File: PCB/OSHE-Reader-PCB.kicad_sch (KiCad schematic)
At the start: 2 parts

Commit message: Update OSHE-Reader-PCB.kicad_sch
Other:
- sheet Display Connector ports: added GND; removed none
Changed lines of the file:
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@@
+	(symbol
+		(lib_id "power:GND")
+		(at 99.06 71.12 0)
+		(unit 1)
+		(exclude_from_sim no)
+		(in_bom yes)
+		(on_board yes)
+		(dnp no)
+		(fields_autoplaced yes)
+		(property "Reference" "#PWR011"
+			(at 99.06 77.47 0)
+			(effects
+				(font
+					(size 1.27 1.27)
+				)
+				(hide yes)
+			)
+		)
+		(property "Value" "GND"
+			(at 99.06 76.2 0)
+			(effects
+				(font
+					(size 1.27 1.27)
+				)
+			)
+		)
+		(property "Footprint" ""
+			(at 99.06 71.12 0)
+			(effects
+				(font
+					(size 1.27 1.27)
+				)
+				(hide yes)
+			)
+		)
+		(property "Datasheet" ""
+			(at 99.06 71.12 0)
+			(effects
+				(font
+					(size 1.27 1.27)
+				)
+				(hide yes)
+			)
+		)
+		(property "Description" "Power symbol creates a global label with name \"GND\" , ground"
+			(at 99.06 71.12 0)
+			(effects
+				(font
+					(size 1.27 1.27)
+				)
+				(hide yes)
+			)
+		)
+		(pin "1"
+		)
+		(instances
+			(project ""
+				(path "/3f072c92-e35a-4654-839b-728bd3dc3a46"
+					(reference "#PWR011")
+					(unit 1)
+				)
+			)
+		)
+	)
 	(symbol
 		(lib_id "power:GND")
@@
 			)
 		)
+		(pin "GND" input
+			(at 103.505 64.77 180)
+			(effects
+				(font
+					(size 1.27 1.27)
+				)
+				(justify left)
+			)
+		)

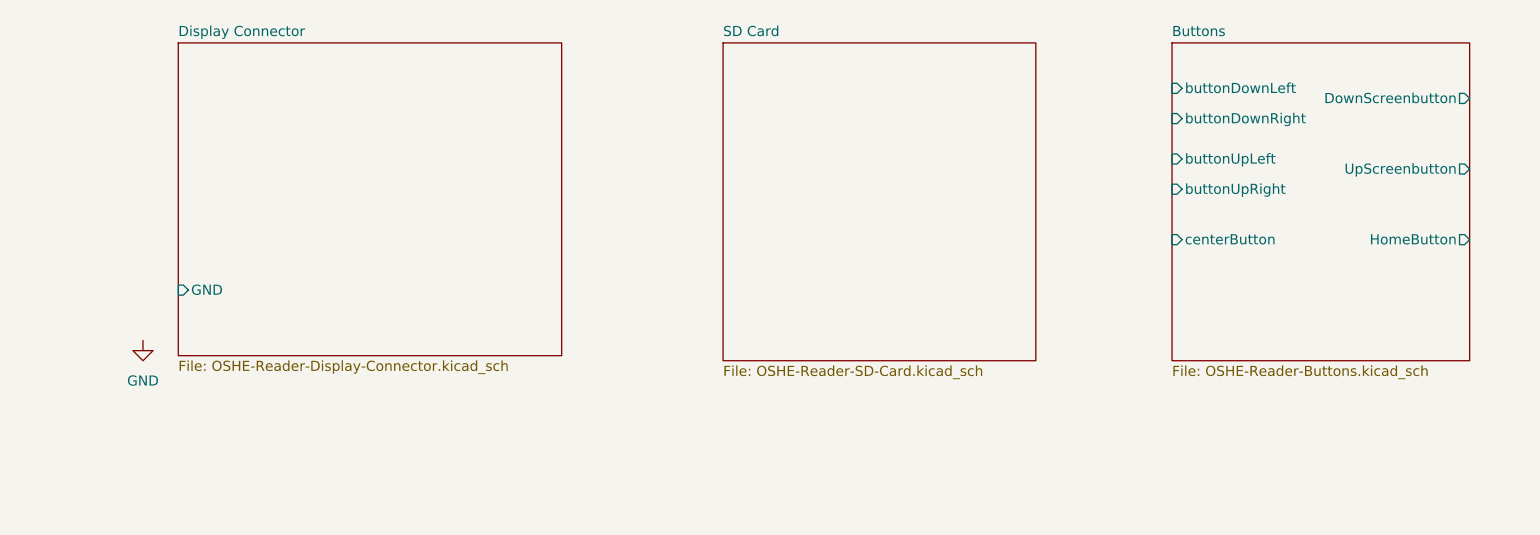
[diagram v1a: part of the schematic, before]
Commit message: Updating pins in roots file
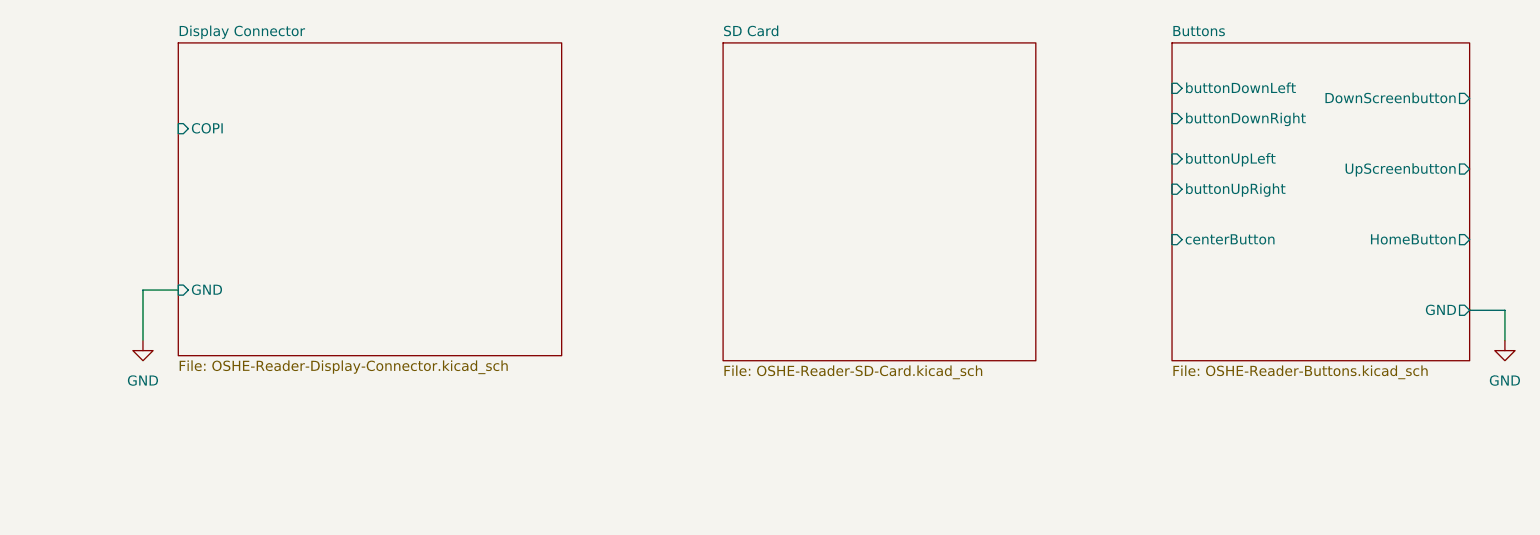
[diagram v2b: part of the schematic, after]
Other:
- sheet Buttons ports: added GND; removed none
- sheet Display Connector ports: added COPI; removed none
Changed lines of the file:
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@@
+	(wire
+		(pts
+			(xy 99.06 64.77) (xy 103.505 64.77)
+		)
+		(stroke
+			(width 0)
+			(type default)
+		)
+	)
 	(wire
 		(pts
@@
 	(wire
 		(pts
+			(xy 270.51 71.12) (xy 270.51 67.31)
+		)
+		(stroke
+			(width 0)
+			(type default)
+		)
+	)
+	(wire
+		(pts
 			(xy 90.17 166.37) (xy 92.71 166.37)
 		)
@@
 	(wire
 		(pts
+			(xy 99.06 64.77) (xy 99.06 71.12)
+		)
+		(stroke
+			(width 0)
+			(type default)
+		)
+	)
+	(wire
+		(pts
 			(xy 104.14 137.16) (xy 101.6 137.16)
 		)
@@
 		(pts
 			(xy 154.94 137.16) (xy 157.48 137.16)
+		)
+		(stroke
+			(width 0)
+			(type default)
+		)
+	)
+	(wire
+		(pts
+			(xy 270.51 67.31) (xy 266.065 67.31)
 		)
 		(stroke
@@
 	(symbol
 		(lib_id "power:GND")
+		(at 270.51 71.12 0)
+		(unit 1)
+		(exclude_from_sim no)
+		(in_bom yes)
+		(on_board yes)
+		(dnp no)
+		(fields_autoplaced yes)
+		(property "Reference" "#PWR06"
+			(at 270.51 77.47 0)
+			(effects
+				(font
+					(size 1.27 1.27)
+				)
+				(hide yes)
+			)
+		)
+		(property "Value" "GND"
+			(at 270.51 76.2 0)
+			(effects
+				(font
+					(size 1.27 1.27)
+				)
+			)
+		)
+		(property "Footprint" ""
+			(at 270.51 71.12 0)
+			(effects
+				(font
+					(size 1.27 1.27)
+				)
+				(hide yes)
+			)
+		)
+		(property "Datasheet" ""
+			(at 270.51 71.12 0)
+			(effects
+				(font
+					(size 1.27 1.27)
+				)
+				(hide yes)
+			)
+		)
+		(property "Description" "Power symbol creates a global label with name \"GND\" , ground"
+			(at 270.51 71.12 0)
+			(effects
+				(font
+					(size 1.27 1.27)
+				)
+				(hide yes)
+			)
+		)
+		(pin "1"
+		)
+		(instances
+			(project "OSHE-Reader-PCB"
+				(path "/3f072c92-e35a-4654-839b-728bd3dc3a46"
+					(reference "#PWR06")
+					(unit 1)
+				)
+			)
+		)
+	)
+	(symbol
+		(lib_id "power:GND")
 		(at 101.6 139.7 0)
 		(unit 1)
@@
 			)
 		)
+		(pin "GND" output
+			(at 266.065 67.31 0)
+			(effects
+				(font
+					(size 1.27 1.27)
+				)
+				(justify right)
+			)
+		)
 		(instances
 			(project "OSHE-Reader-PCB"
@@
 			(effects
 				(font
+					(size 1.27 1.27)
+				)
+				(justify left)
+			)
+		)
+		(pin "COPI" input
+			(at 103.505 44.45 180)
+			(effects
+				(font

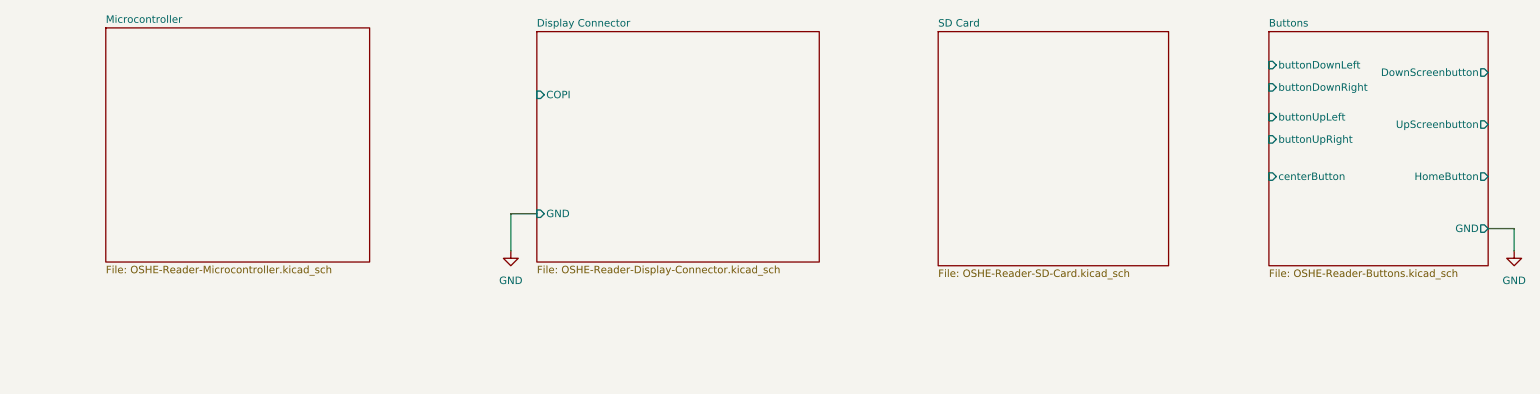
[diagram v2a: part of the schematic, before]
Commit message: updated sd card main sheet pins, swapped big caps for small ones on display connector for better readability
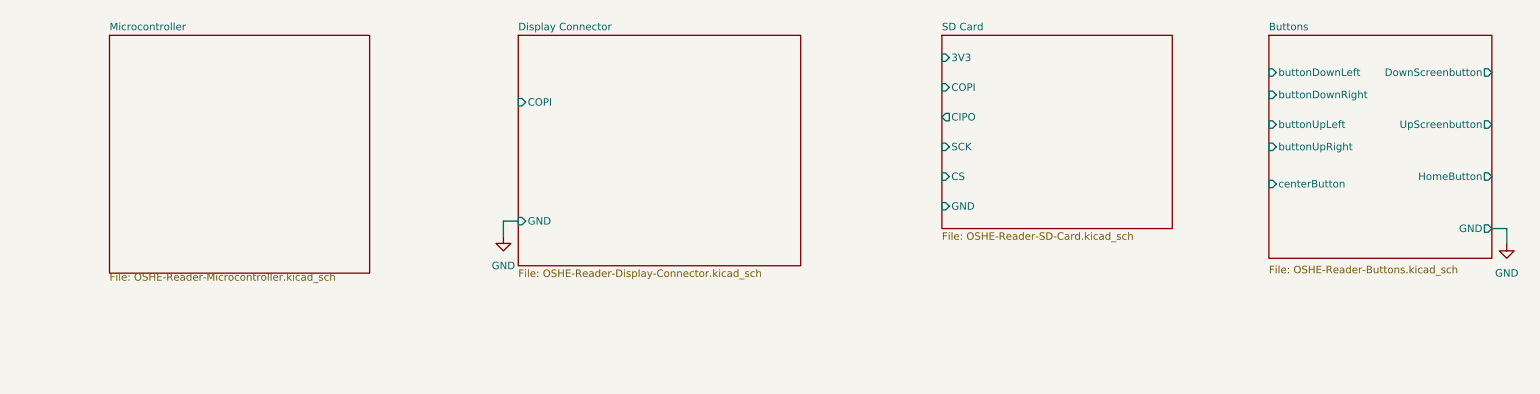
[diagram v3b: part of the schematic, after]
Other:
- sheet SD Card ports: added 3V3, CIPO, COPI, CS, GND, SCK; removed none
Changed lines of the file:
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@@
+	(wire
+		(pts
+			(xy 269.24 67.31) (xy 266.7 67.31)
+		)
+		(stroke
+			(width 0)
+			(type default)
+		)
+	)
 	(wire
 		(pts
@@
 	(wire
 		(pts
-			(xy 99.06 64.77) (xy 103.505 64.77)
-		)
-		(stroke
-			(width 0)
-			(type default)
-		)
-	)
-	(wire
-		(pts
 			(xy 87.63 166.37) (xy 87.63 162.56)
 		)
@@
 	(wire
 		(pts
+			(xy 100.33 66.04) (xy 97.79 66.04)
+		)
+		(stroke
+			(width 0)
+			(type default)
+		)
+	)
+	(wire
+		(pts
 			(xy 87.63 154.94) (xy 87.63 129.54)
 		)
@@
 	(wire
 		(pts
+			(xy 269.24 69.85) (xy 269.24 67.31)
+		)
+		(stroke
+			(width 0)
+			(type default)
+		)
+	)
+	(wire
+		(pts
 			(xy 30.48 137.16) (xy 33.02 137.16)
 		)
@@
 	(wire
 		(pts
-			(xy 270.51 71.12) (xy 270.51 67.31)
-		)
-		(stroke
-			(width 0)
-			(type default)
-		)
-	)
-	(wire
-		(pts
 			(xy 90.17 166.37) (xy 92.71 166.37)
 		)
@@
 	(wire
 		(pts
-			(xy 99.06 64.77) (xy 99.06 71.12)
-		)
-		(stroke
-			(width 0)
-			(type default)
-		)
-	)
-	(wire
-		(pts
 			(xy 104.14 137.16) (xy 101.6 137.16)
 		)
@@
 	(wire
 		(pts
-			(xy 270.51 67.31) (xy 266.065 67.31)
+			(xy 97.79 66.04) (xy 97.79 68.58)
 		)
 		(stroke
@@
 	(symbol
 		(lib_id "power:GND")
-		(at 99.06 71.12 0)
+		(at 97.79 68.58 0)
 		(unit 1)
 		(exclude_from_sim no)
@@
 		(fields_autoplaced yes)
 		(property "Reference" "#PWR011"
-			(at 99.06 77.47 0)
+			(at 97.79 74.93 0)
 			(effects
 				(font
@@
 		)
 		(property "Value" "GND"
-			(at 99.06 76.2 0)
+			(at 97.79 73.66 0)
 			(effects
 				(font
@@
 		)
 		(property "Footprint" ""
-			(at 99.06 71.12 0)
+			(at 97.79 68.58 0)
 			(effects
 				(font
@@
 		)
 		(property "Datasheet" ""
-			(at 99.06 71.12 0)
+			(at 97.79 68.58 0)
 			(effects
 				(font
@@
 		)
 		(property "Description" "Power symbol creates a global label with name \"GND\" , ground"
-			(at 99.06 71.12 0)
+			(at 97.79 68.58 0)
 			(effects
 				(font
@@
 	(symbol
 		(lib_id "power:GND")
-		(at 270.51 71.12 0)
+		(at 269.24 69.85 0)
 		(unit 1)
 		(exclude_from_sim no)
@@
 		(fields_autoplaced yes)
 		(property "Reference" "#PWR06"
-			(at 270.51 77.47 0)
+			(at 269.24 76.2 0)
 			(effects
 				(font
@@
 		)
 		(property "Value" "GND"
-			(at 270.51 76.2 0)
+			(at 269.24 74.93 0)
 			(effects
 				(font
@@
 		)
 		(property "Footprint" ""
-			(at 270.51 71.12 0)
+			(at 269.24 69.85 0)
 			(effects
 				(font
@@
 		)
 		(property "Datasheet" ""
-			(at 270.51 71.12 0)
+			(at 269.24 69.85 0)
 			(effects
 				(font
@@
 		)
 		(property "Description" "Power symbol creates a global label with name \"GND\" , ground"
-			(at 270.51 71.12 0)
+			(at 269.24 69.85 0)
 			(effects
 				(font
@@
 	)
 	(sheet
-		(at 29.845 33.02)
-		(size 45.085 40.005)
+		(at 30.48 34.29)
+		(size 44.45 40.64)
 		(exclude_from_sim no)
 		(in_bom yes)
@@
 		)
 		(property "Sheetname" "Microcontroller"
-			(at 29.845 32.3084 0)
+			(at 30.48 33.5784 0)
 			(effects
 				(font
@@
 		)
 		(property "Sheetfile" "OSHE-Reader-Microcontroller.kicad_sch"
-			(at 29.845 73.6096 0)
+			(at 30.48 74.8796 0)
 			(effects
 				(font
@@
 	)
 	(sheet
-		(at 228.6 33.655)
-		(size 37.465 40.005)
+		(at 228.6 34.29)
+		(size 38.1 38.1)
 		(exclude_from_sim no)
 		(in_bom yes)
@@
 		)
 		(property "Sheetname" "Buttons"
-			(at 228.6 32.9434 0)
+			(at 228.6 33.5784 0)
 			(effects
 				(font
@@
 		)
 		(property "Sheetfile" "OSHE-Reader-Buttons.kicad_sch"
-			(at 228.6 74.2446 0)
+			(at 228.6 73.6096 0)
 			(effects
 				(font
@@
 		)
 		(pin "buttonDownLeft" input
-			(at 228.6 39.37 180)
+			(at 228.6 40.64 180)
 			(effects
 				(font
@@
 		)
 		(pin "buttonUpLeft" input
-			(at 228.6 48.26 180)
+			(at 228.6 49.53 180)
 			(effects
 				(font
@@
 		)
 		(pin "centerButton" input
-			(at 228.6 58.42 180)
+			(at 228.6 59.69 180)
 			(effects
 				(font
@@
 		)
 		(pin "buttonDownRight" input
-			(at 228.6 43.18 180)
+			(at 228.6 44.45 180)
 			(effects
 				(font
@@
 		)
 		(pin "buttonUpRight" input
-			(at 228.6 52.07 180)
+			(at 228.6 53.34 180)
 			(effects
 				(font
@@
 		)
 		(pin "DownScreenbutton" output
-			(at 266.065 40.64 0)
+			(at 266.7 40.64 0)
 			(effects
 				(font
@@
 		)
 		(pin "HomeButton" output
-			(at 266.065 58.42 0)
+			(at 266.7 58.42 0)
 			(effects
 				(font
@@
 		)
 		(pin "UpScreenbutton" output
-			(at 266.065 49.53 0)
+			(at 266.7 49.53 0)
 			(effects
 				(font
@@
 		)
 		(pin "GND" output
-			(at 266.065 67.31 0)
+			(at 266.7 67.31 0)
 			(effects
 				(font
@@
 	)
 	(sheet
-		(at 103.505 33.655)
+		(at 100.33 34.29)
 		(size 48.26 39.37)
 		(exclude_from_sim no)
@@
 		)
 		(property "Sheetname" "Display Connector"
-			(at 103.505 32.9434 0)
+			(at 100.33 33.5784 0)
 			(effects
 				(font
@@
 		)
 		(property "Sheetfile" "OSHE-Reader-Display-Connector.kicad_sch"
-			(at 103.505 73.6096 0)
+			(at 100.33 74.2446 0)
 			(effects
 				(font
@@
 		)
 		(pin "GND" input
-			(at 103.505 64.77 180)
+			(at 100.33 66.04 180)
 			(effects
 				(font
@@
 		)
 		(pin "COPI" input
-			(at 103.505 44.45 180)
+			(at 100.33 45.72 180)
 			(effects
 				(font
@@
 	)
 	(sheet
-		(at 172.085 33.655)
-		(size 39.37 40.005)
+		(at 172.72 34.29)
+		(size 39.37 33.02)
 		(exclude_from_sim no)
 		(in_bom yes)
@@
 		)
 		(property "Sheetname" "SD Card"
-			(at 172.085 32.9434 0)
+			(at 172.72 33.5784 0)
 			(effects
 				(font
@@
 		)
 		(property "Sheetfile" "OSHE-Reader-SD-Card.kicad_sch"
-			(at 172.085 74.2446 0)
+			(at 172.72 67.8946 0)
 			(effects
 				(font
@@
 			)
 		)
+		(pin "CS" input
+			(at 172.72 58.42 180)
+			(effects
+				(font
+					(size 1.27 1.27)
+				)
+				(justify left)
+			)
+		)
+		(pin "SCK" input
+			(at 172.72 53.34 180)
+			(effects
+				(font
+					(size 1.27 1.27)
+				)
+				(justify left)
+			)
+		)
+		(pin "3V3" input
+			(at 172.72 38.1 180)
+			(effects
+				(font
+					(size 1.27 1.27)
+				)
+				(justify left)
+			)
+		)
+		(pin "CIPO" output
+			(at 172.72 48.26 180)
+			(effects
+				(font
+					(size 1.27 1.27)
+				)
+				(justify left)
+			)
+		)
+		(pin "COPI" input
+			(at 172.72 43.18 180)
+			(effects
+				(font
+					(size 1.27 1.27)
+				)
+				(justify left)
+			)
+		)
+		(pin "GND" input
+			(at 172.72 63.5 180)
+			(effects
+				(font
+					(size 1.27 1.27)
+				)
+				(justify left)
+			)
+		)

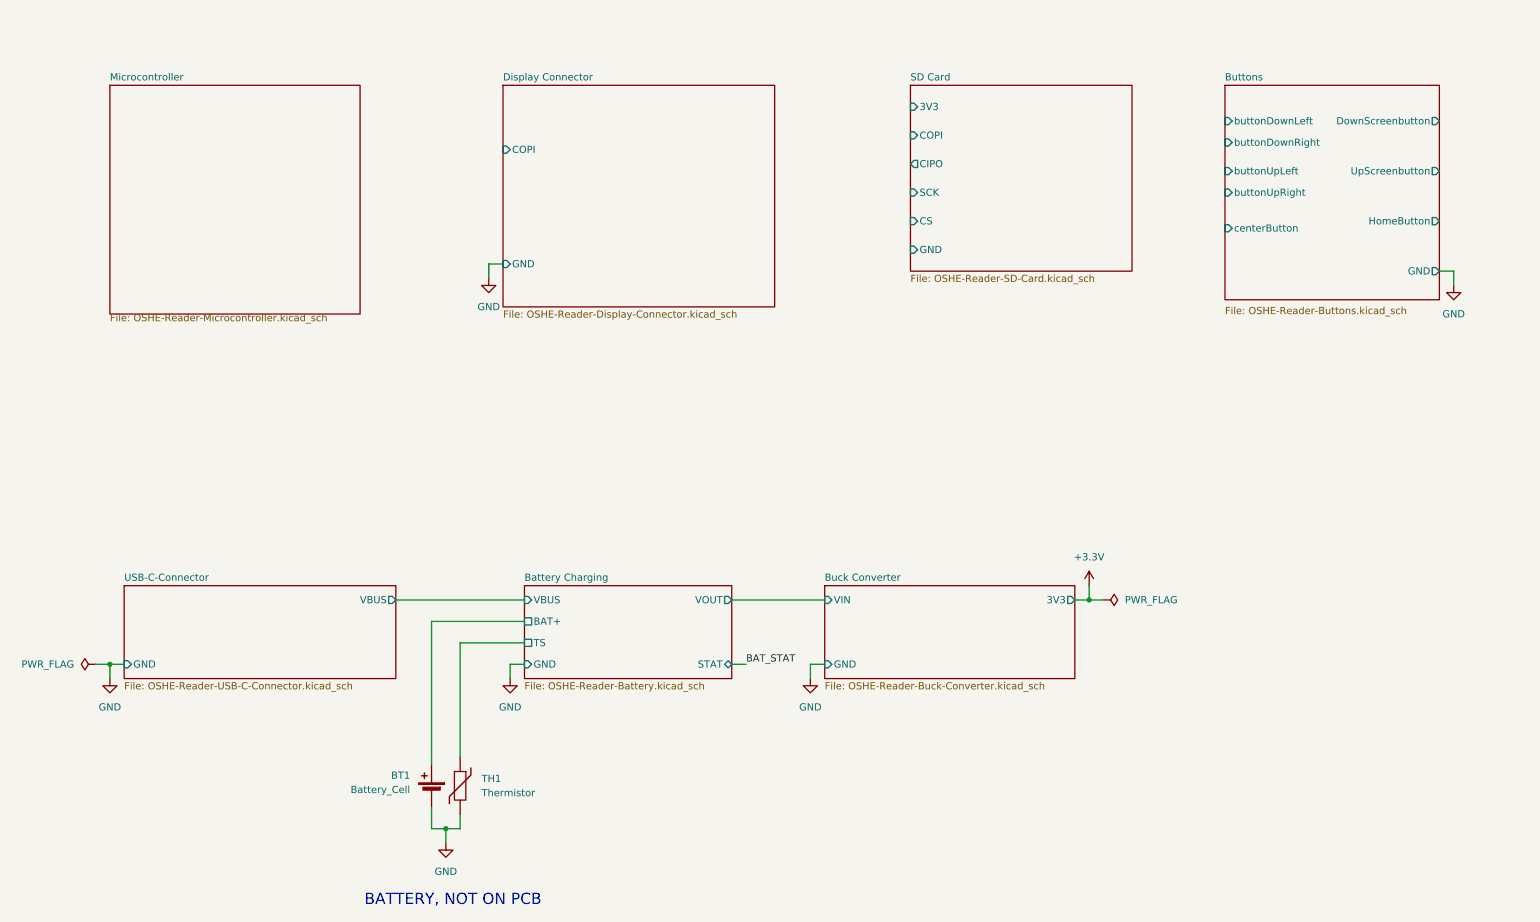
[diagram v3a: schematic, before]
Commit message: cleaned up main sheet and synced labels for presentation
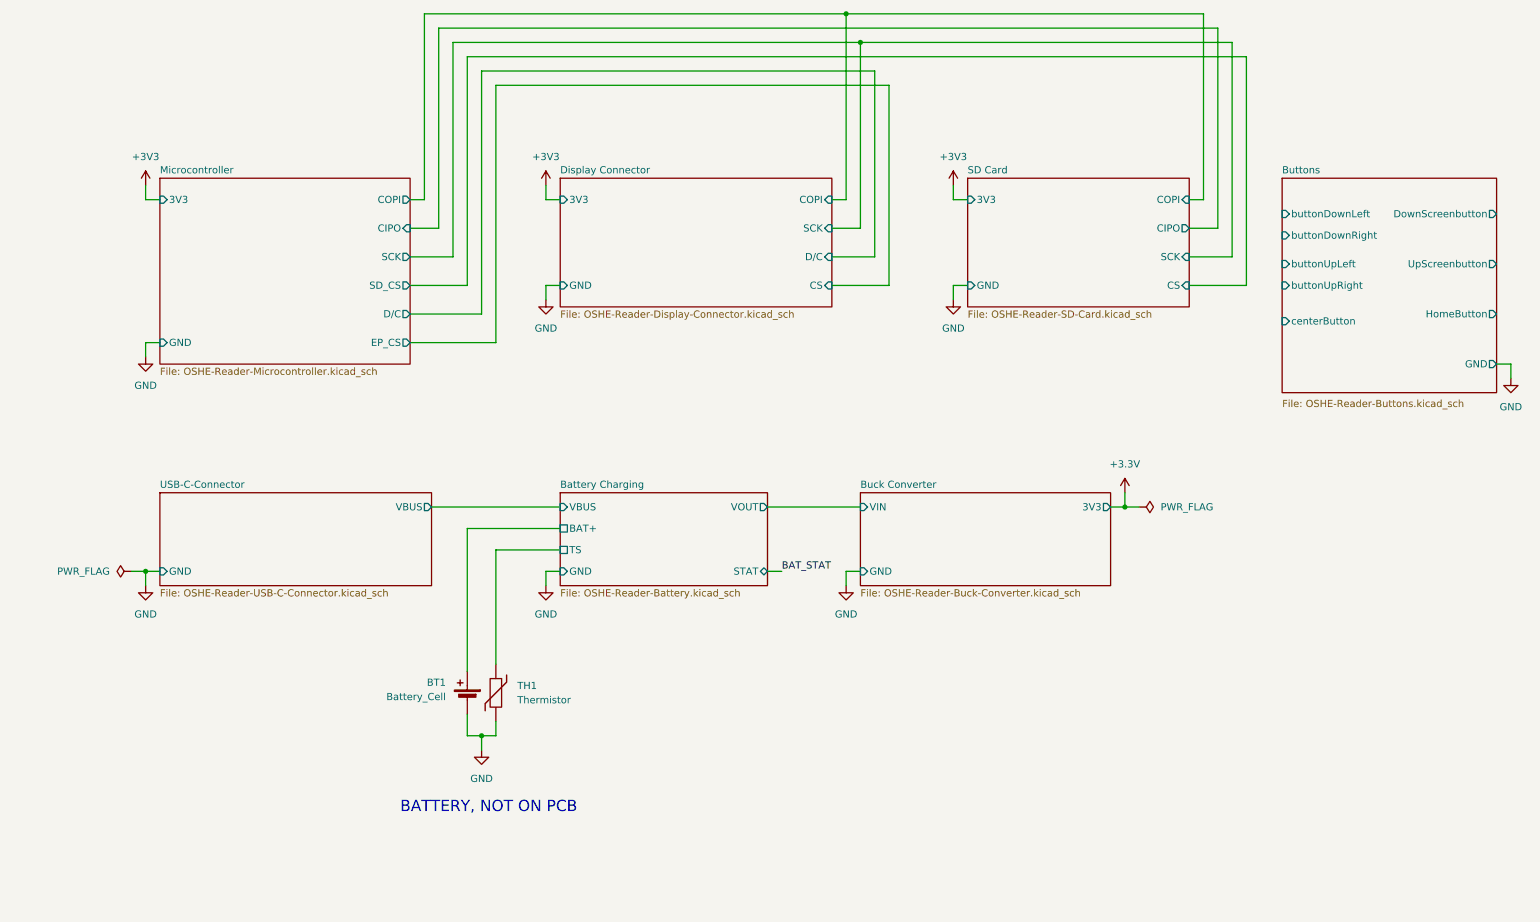
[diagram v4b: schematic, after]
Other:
- sheet Display Connector ports: added 3V3, CS, D/C, SCK; removed none
- sheet Microcontroller ports: added 3V3, CIPO, COPI, D/C, EP_CS, GND, SCK, SD_CS; removed none
- moved on the sheet: BT1, TH1
